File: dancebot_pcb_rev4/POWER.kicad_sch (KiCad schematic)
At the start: 28 parts, among them IC201 TPS63000IDRCRQ1, J201 BatteryJ ST Connector

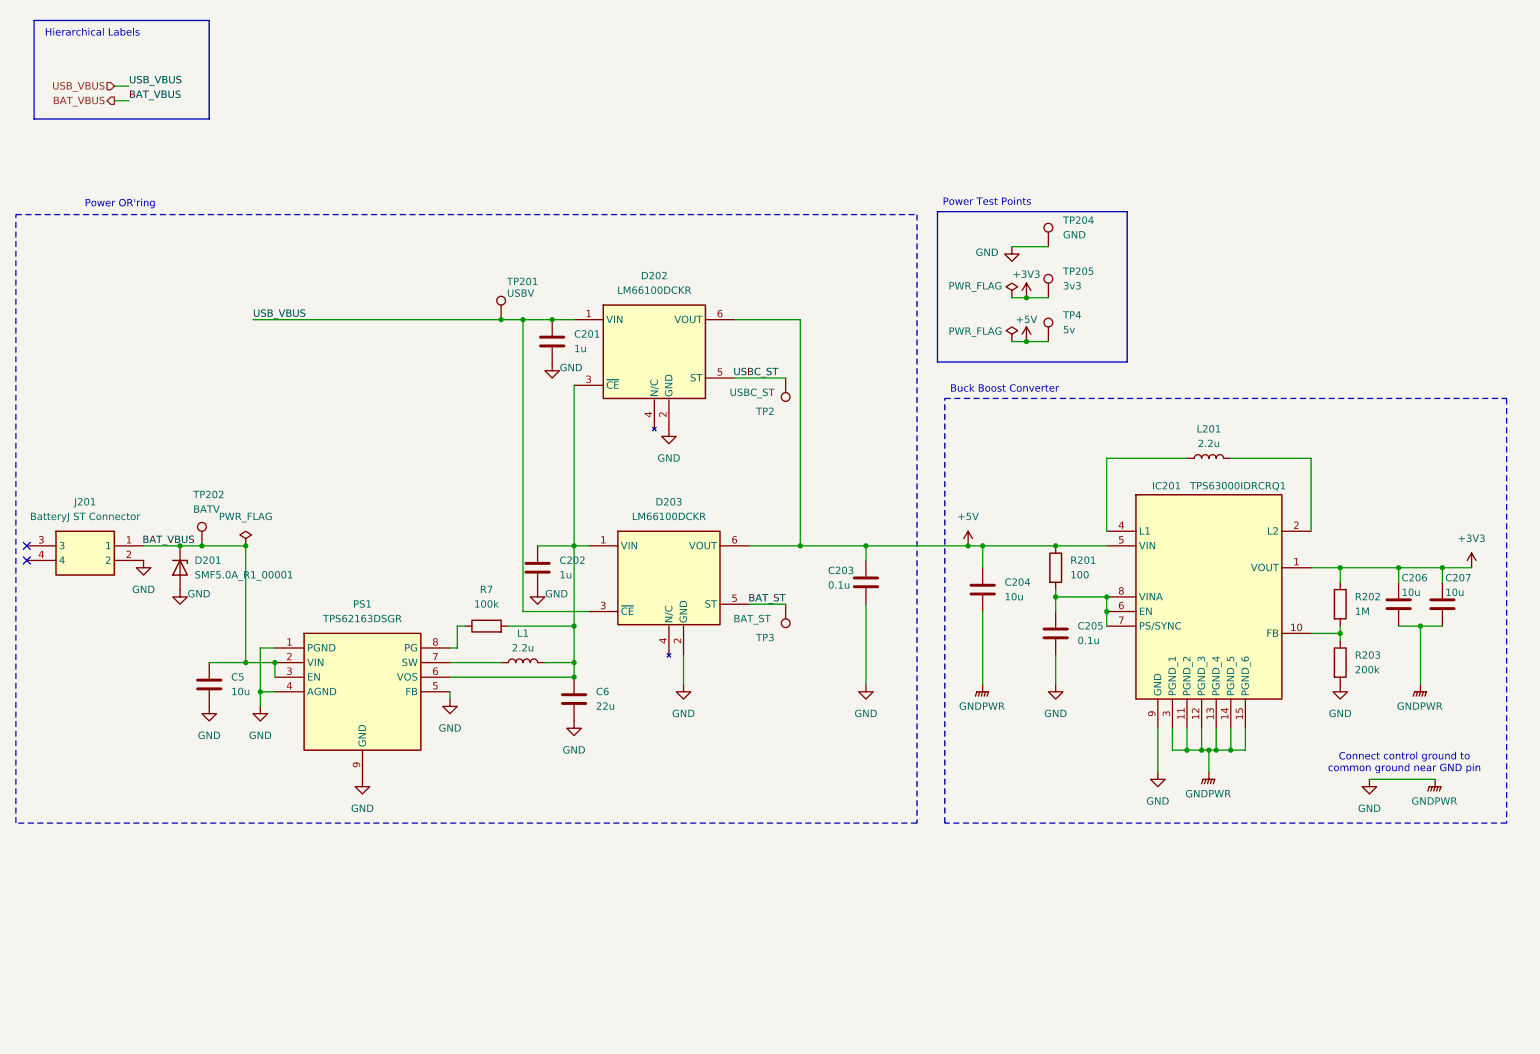
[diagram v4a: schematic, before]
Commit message: added more power leds. need to finish routing. fixed 3d models
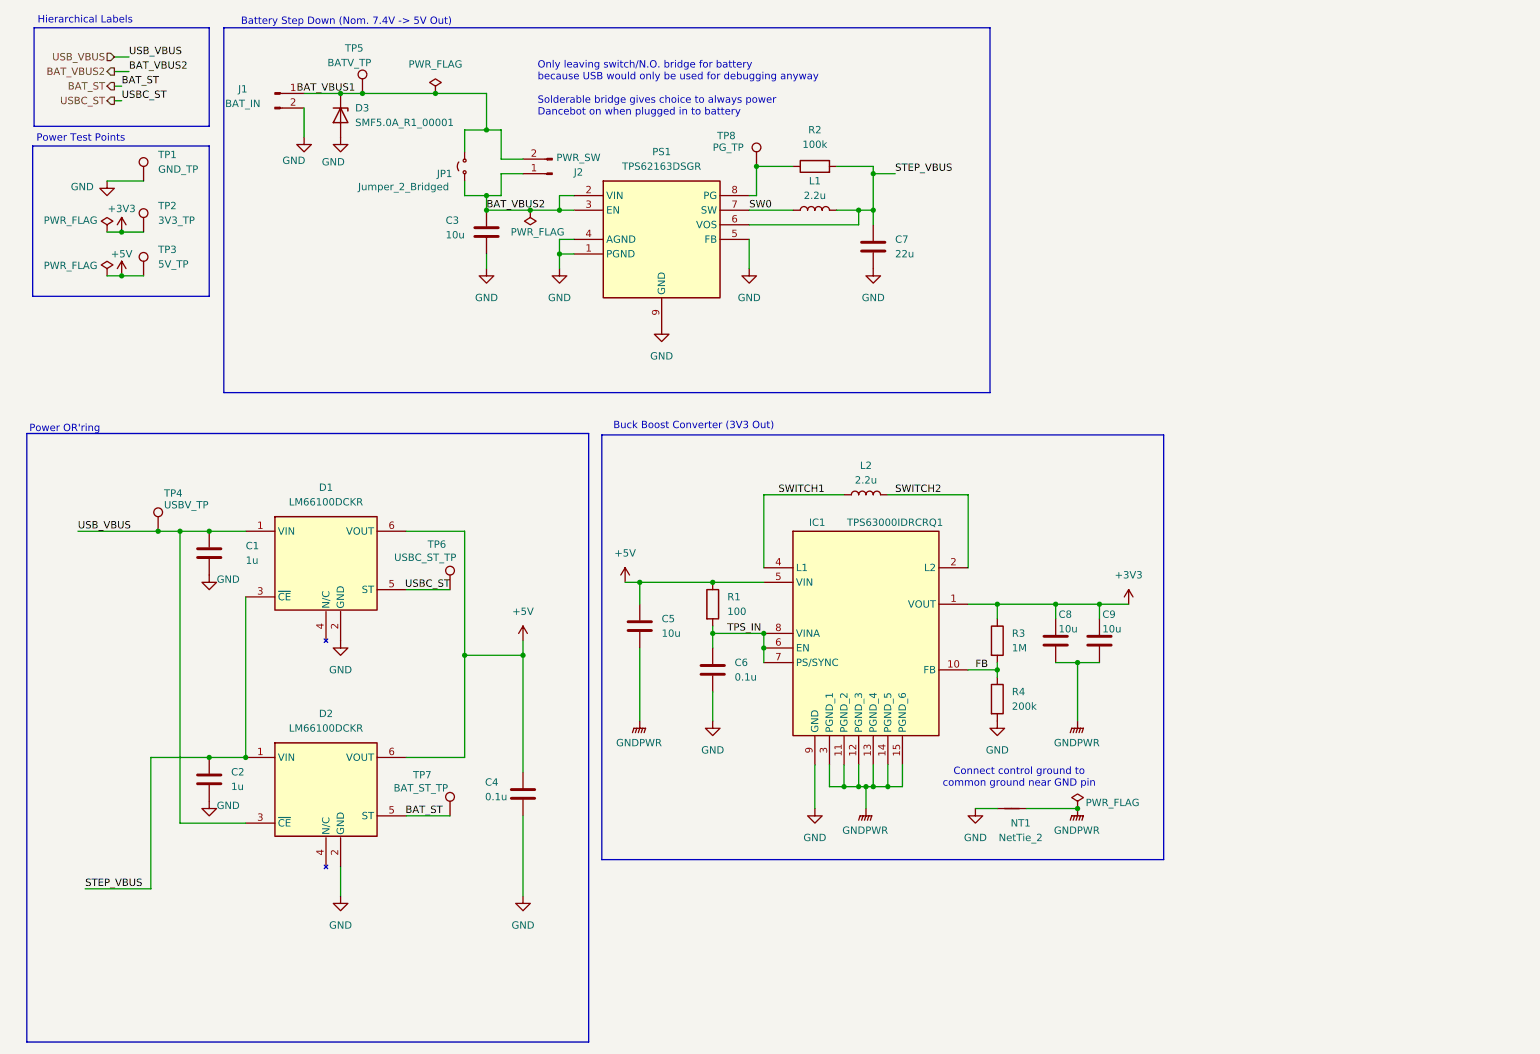
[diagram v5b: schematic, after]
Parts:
- removed C5: 10u, SamacSys_Parts:CAPC1608X80N, symbol Device:C
- removed J201: BatteryJ ST Connector, SamacSys_Parts:1769, symbol SamacSys_Parts:1769
- removed R7: 100k, SamacSys_Parts:RESC2012X50N, symbol Device:R
- added C3: 10u, SamacSys_Parts:CAPC1608X80N, symbol Device:C
- added J1: BAT_IN, Connector_PinHeader_2.00mm:PinHeader_1x02_P2.00mm_Vertical, symbol Connector:Conn_01x02_Pin
- added J2: PWR_SW, Connector_PinHeader_2.00mm:PinHeader_1x02_P2.00mm_Vertical, symbol Connector:Conn_01x02_Pin
- added JP1: Jumper_2_Bridged, Jumper:SolderJumper-2_P1.3mm_Open_RoundedPad1.0x1.5mm, symbol Jumper:Jumper_2_Small_Open
- added NT1: NetTie_2, NetTie:NetTie-2_SMD_Pad0.5mm, symbol Device:NetTie_2
- added R2: 100k, SamacSys_Parts:RESC2012X50N, symbol Device:R
- added TP8: PG_TP, SamacSys_Parts:TestPoint_Pad_1.0x1.0mm, symbol Connector:TestPoint
- C4: renamed from C203; footprint SamacSys_Parts:MAJx16 -> SamacSys_Parts:CAPC2012X140N; Height 0.8 -> 1.4; Manufacturer_Name TAIYO YUDEN -> Kyocera AVX; Manufacturer_Part_Number MAJCU168BB7104KTEA01 -> KAF21KR72A104KL; Mouser Part Number 963-MAJCH168BB7104KT -> 581-KAF21KR72A104KL; Mouser Price/Stock https://www.mouser.co.uk/ProductDetail/TAIYO-YUDEN/MAJCH168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 -> https://www.mouser.co.uk/ProductDetail/KYOCERA-AVX/KAF21KR7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
- C6: renamed from C205; footprint SamacSys_Parts:MAJx16 -> SamacSys_Parts:CAPC2012X140N; Height 0.8 -> 1.4; Manufacturer_Name TAIYO YUDEN -> Kyocera AVX; Manufacturer_Part_Number MAJCU168BB7104KTEA01 -> KAF21KR72A104KL; Mouser Part Number 963-MAJCH168BB7104KT -> 581-KAF21KR72A104KL; Mouser Price/Stock https://www.mouser.co.uk/ProductDetail/TAIYO-YUDEN/MAJCH168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 -> https://www.mouser.co.uk/ProductDetail/KYOCERA-AVX/KAF21KR7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
- C7: renamed from C6; Height (none) -> 1.45; Manufacturer_Name (none) -> TAIYO YUDEN; Manufacturer_Part_Number (none) -> JMK212BBJ226MG8T; Mouser Part Number (none) -> 963-JMK212BBJ226MG8T; Mouser Price/Stock (none) -> https://www.mouser.co.uk/ProductDetail/TAIYO-YUDEN/JMK212BB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
- R4: renamed from R203; footprint SamacSys_Parts:RESC1608X55N -> SamacSys_Parts:RESC2012X60N; Height 0.55 -> 0.6; Manufacturer_Name ROHM Semiconductor -> KOA Speer; Manufacturer_Part_Number KTR03EZPJ204 -> SG73P2ATTD2003F; Mouser Part Number 755-KTR03EZPJ204 -> 660-SG73P2ATTD2003F; Mouser Price/Stock https://www.mouser.co.uk/ProductDetail/ROHM-Semiconductor/K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 -> https://www.mouser.co.uk/ProductDetail/KOA-Speer/SG73P2ATTD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
- TP1: renamed from TP204; value GND -> GND_TP; footprint TestPoint:TestPoint_Pad_1.0x1.0mm -> SamacSys_Parts:TestPoint_Pad_1.0x1.0mm
- TP2: renamed from TP205; value 3v3 -> 3V3_TP; footprint TestPoint:TestPoint_Pad_1.0x1.0mm -> SamacSys_Parts:TestPoint_Pad_1.0x1.0mm
- TP3: renamed from TP4; value 5v -> 5V_TP; footprint TestPoint:TestPoint_Pad_1.0x1.0mm -> SamacSys_Parts:TestPoint_Pad_1.0x1.0mm
- TP4: renamed from TP201; value USBV -> USBV_TP; footprint TestPoint:TestPoint_Pad_1.0x1.0mm -> SamacSys_Parts:TestPoint_Pad_1.0x1.0mm
- TP5: renamed from TP202; value BATV -> BATV_TP; footprint TestPoint:TestPoint_Pad_1.0x1.0mm -> SamacSys_Parts:TestPoint_Pad_1.0x1.0mm
- TP6: renamed from TP2; value USBC_ST -> USBC_ST_TP; footprint TestPoint:TestPoint_Pad_1.0x1.0mm -> SamacSys_Parts:TestPoint_Pad_1.0x1.0mm
- TP7: renamed from TP3; value BAT_ST -> BAT_ST_TP; footprint TestPoint:TestPoint_Pad_1.0x1.0mm -> SamacSys_Parts:TestPoint_Pad_1.0x1.0mm
- renumbered C201 to C1, C202 to C2, C204 to C5, C206 to C8, C207 to C9, D202 to D1, D203 to D2, D201 to D3, IC201 to IC1, L201 to L2, R201 to R1, R202 to R3
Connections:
- net GND: now also C3.2, J1.2 (Pin_2), NT1.1; no longer C5.2, C8.2, C9.2, IC1.11 (PGND_2), IC1.12 (PGND_3), IC1.13 (PGND_4), IC1.14 (PGND_5), IC1.15 (PGND_6), IC1.3 (PGND_1)
- net SW0: now reaches L1.1, PS1.7 (SW)
- net STEP_VBUS: now reaches C2.1, C7.1, D1.3 (~{CE}), D2.1 (VIN), L1.2, PS1.6 (VOS)
- net STEP_VBUS: now also R2.2
- net FB: now reaches IC1.10 (FB), R3.2, R4.1
- net TPS_IN: now reaches C6.1, IC1.6 (EN), IC1.7 (PS/SYNC), IC1.8 (VINA), R1.2
- net at PS1.8 (PG): now also R2.1, TP8.1
- net SWITCH1: now reaches IC1.4 (L1), L2.1
- net SWITCH2: now reaches IC1.2 (L2), L2.2
- net BAT_VBUS renamed BAT_VBUS1
- net BAT_VBUS1: now also J1.1 (Pin_1), J2.2 (Pin_2), JP1.2 (B); no longer PS1.2 (VIN), PS1.3 (EN)
- new net BAT_VBUS2: C3.1, J2.1 (Pin_1), JP1.1 (A), PS1.2 (VIN), PS1.3 (EN)
- new net GNDPWR: C5.2, C8.2, C9.2, IC1.11 (PGND_2), IC1.12 (PGND_3), IC1.13 (PGND_4), IC1.14 (PGND_5), IC1.15 (PGND_6), IC1.3 (PGND_1), NT1.2
- no-connect marks 2 -> 0
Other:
- note added: "Battery Step Down (Nom. 7.4V -> 5V Out)"
- note added: "Buck Boost Converter (3V3 Out)"
- note added: "Only leaving switch/N.O. bridge for battery because USB would only be used for debugging anyway Solderable bridge gives choice to always power Dancebot on when plugged in to battery"
- note removed: "Buck Boost Converter"
- moved on the sheet: C1, C2, C4, C5, C6, C7, C8, C9, D1, D2, D3, IC1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

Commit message: finished first layout. need to add polygon pours
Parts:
- NT1: footprint NetTie:NetTie-2_SMD_Pad0.5mm -> SamacSys_Parts:NetTie-2_SMD_Pad0.3mm
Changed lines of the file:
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@@
 		(on_board yes)
 		(dnp no)
-		(property "Reference" "#PWR04"
+		(property "Reference" "#PWR08"
 			(at 46.99 118.11 0)
 			(effects
@@
 			(project "Dancebot_PCB"
 				(path "/21324b60-e5e7-4de6-a38d-f4cdf81a1b2c/9bb1d94d-135a-4bfe-a8c4-60fef77f5043"
-					(reference "#PWR04")
+					(reference "#PWR08")
 					(unit 1)
 				)
@@
 		(on_board yes)
 		(dnp no)
-		(property "Reference" "#PWR07"
+		(property "Reference" "#PWR011"
 			(at 69.85 41.91 0)
 			(effects
@@
 			(project "Dancebot_PCB"
 				(path "/21324b60-e5e7-4de6-a38d-f4cdf81a1b2c/9bb1d94d-135a-4bfe-a8c4-60fef77f5043"
-					(reference "#PWR07")
+					(reference "#PWR011")
 					(unit 1)
 				)
@@
 		(on_board yes)
 		(dnp no)
-		(property "Reference" "#PWR05"
+		(property "Reference" "#PWR09"
 			(at 46.99 157.48 0)
 			(effects
@@
 			(project "Dancebot_PCB"
 				(path "/21324b60-e5e7-4de6-a38d-f4cdf81a1b2c/9bb1d94d-135a-4bfe-a8c4-60fef77f5043"
-					(reference "#PWR05")
+					(reference "#PWR09")
 					(unit 1)
 				)
@@
 		(dnp no)
 		(fields_autoplaced yes)
-		(property "Reference" "#PWR025"
+		(property "Reference" "#PWR029"
 			(at 198.12 157.48 0)
 			(effects
@@
 			(project "Dancebot_PCB"
 				(path "/21324b60-e5e7-4de6-a38d-f4cdf81a1b2c/9bb1d94d-135a-4bfe-a8c4-60fef77f5043"
-					(reference "#PWR025")
+					(reference "#PWR029")
 					(unit 1)
 				)
@@
 		(on_board yes)
 		(dnp no)
-		(property "Reference" "#FLG05"
+		(property "Reference" "#FLG04"
 			(at 102.87 50.165 0)
 			(effects
@@
 			(project "Dancebot_PCB"
 				(path "/21324b60-e5e7-4de6-a38d-f4cdf81a1b2c/9bb1d94d-135a-4bfe-a8c4-60fef77f5043"
-					(reference "#FLG05")
+					(reference "#FLG04")
 					(unit 1)
 				)
@@
 		(dnp no)
 		(fields_autoplaced yes)
-		(property "Reference" "#PWR08"
+		(property "Reference" "#PWR012"
 			(at 69.85 129.54 0)
 			(effects
@@
 			(project "Dancebot_PCB"
 				(path "/21324b60-e5e7-4de6-a38d-f4cdf81a1b2c/9bb1d94d-135a-4bfe-a8c4-60fef77f5043"
-					(reference "#PWR08")
+					(reference "#PWR012")
 					(unit 1)
 				)
@@
 		(on_board yes)
 		(dnp no)
-		(property "Reference" "#PWR06"
+		(property "Reference" "#PWR010"
 			(at 63.5 41.91 0)
 			(effects
@@
 			(project "Dancebot_PCB"
 				(path "/21324b60-e5e7-4de6-a38d-f4cdf81a1b2c/9bb1d94d-135a-4bfe-a8c4-60fef77f5043"
-					(reference "#PWR06")
+					(reference "#PWR010")
 					(unit 1)
 				)
@@
 		(on_board yes)
 		(dnp no)
-		(property "Reference" "#PWR01"
+		(property "Reference" "#PWR05"
 			(at 29.21 49.53 0)
 			(effects
@@
 			(project "Dancebot_PCB"
 				(path "/21324b60-e5e7-4de6-a38d-f4cdf81a1b2c/9bb1d94d-135a-4bfe-a8c4-60fef77f5043"
-					(reference "#PWR01")
+					(reference "#PWR05")
 					(unit 1)
 				)
@@
 		(dnp no)
 		(fields_autoplaced yes)
-		(property "Reference" "#PWR024"
+		(property "Reference" "#PWR028"
 			(at 198.12 142.24 0)
 			(effects
@@
 			(project "Dancebot_PCB"
 				(path "/21324b60-e5e7-4de6-a38d-f4cdf81a1b2c/9bb1d94d-135a-4bfe-a8c4-60fef77f5043"
-					(reference "#PWR024")
+					(reference "#PWR028")
 					(unit 1)
 				)
@@
 		(dnp no)
 		(fields_autoplaced yes)
-		(property "Reference" "#PWR09"
+		(property "Reference" "#PWR013"
 			(at 69.85 173.99 0)
 			(effects
@@
 			(project "Dancebot_PCB"
 				(path "/21324b60-e5e7-4de6-a38d-f4cdf81a1b2c/9bb1d94d-135a-4bfe-a8c4-60fef77f5043"
-					(reference "#PWR09")
+					(reference "#PWR013")
 					(unit 1)
 				)
@@
 		(dnp no)
 		(fields_autoplaced yes)
-		(property "Reference" "#PWR010"
+		(property "Reference" "#PWR014"
 			(at 95.25 64.77 0)
 			(effects
@@
 			(project ""
 				(path "/21324b60-e5e7-4de6-a38d-f4cdf81a1b2c/9bb1d94d-135a-4bfe-a8c4-60fef77f5043"
-					(reference "#PWR010")
+					(reference "#PWR014")
 					(unit 1)
 				)
@@
 			)
 		)
-		(property "Footprint" "NetTie:NetTie-2_SMD_Pad0.5mm"
+		(property "Footprint" "SamacSys_Parts:NetTie-2_SMD_Pad0.3mm"
 			(at 186.69 152.4 0)
 			(effects
@@
 		(on_board yes)
 		(dnp no)
-		(property "Reference" "#FLG04"
+		(property "Reference" "#FLG05"
 			(at 198.12 150.495 0)
 			(effects
@@
 			(project "Dancebot_PCB"
 				(path "/21324b60-e5e7-4de6-a38d-f4cdf81a1b2c/9bb1d94d-135a-4bfe-a8c4-60fef77f5043"
-					(reference "#FLG04")
+					(reference "#FLG05")
 					(unit 1)
 				)
@@
 		(dnp no)
 		(fields_autoplaced yes)
-		(property "Reference" "#PWR011"
+		(property "Reference" "#PWR015"
 			(at 101.6 127 0)
 			(effects
@@
 			(project "Dancebot_PCB"
 				(path "/21324b60-e5e7-4de6-a38d-f4cdf81a1b2c/9bb1d94d-135a-4bfe-a8c4-60fef77f5043"
-					(reference "#PWR011")
+					(reference "#PWR015")
 					(unit 1)
 				)
@@
 		(dnp no)
 		(fields_autoplaced yes)
-		(property "Reference" "#PWR018"
+		(property "Reference" "#PWR022"
 			(at 140.97 64.77 0)
 			(effects
@@
 			(project ""
 				(path "/21324b60-e5e7-4de6-a38d-f4cdf81a1b2c/9bb1d94d-135a-4bfe-a8c4-60fef77f5043"
-					(reference "#PWR018")
+					(reference "#PWR022")
 					(unit 1)
 				)
@@
 		(dnp no)
 		(fields_autoplaced yes)
-		(property "Reference" "#PWR023"
+		(property "Reference" "#PWR027"
 			(at 184.15 143.51 0)
 			(effects
@@
 			(project "Dancebot_PCB"
 				(path "/21324b60-e5e7-4de6-a38d-f4cdf81a1b2c/9bb1d94d-135a-4bfe-a8c4-60fef77f5043"
-					(reference "#PWR023")
+					(reference "#PWR027")
 					(unit 1)
 				)
@@
 		(dnp no)
 		(fields_autoplaced yes)
-		(property "Reference" "#PWR020"
+		(property "Reference" "#PWR024"
 			(at 161.29 157.48 0)
 			(effects
@@
 			(project "Dancebot_PCB"
 				(path "/21324b60-e5e7-4de6-a38d-f4cdf81a1b2c/9bb1d94d-135a-4bfe-a8c4-60fef77f5043"
-					(reference "#PWR020")
+					(reference "#PWR024")
 					(unit 1)
 				)
@@
 		(dnp no)
 		(fields_autoplaced yes)
-		(property "Reference" "#PWR019"
+		(property "Reference" "#PWR023"
 			(at 152.4 158.75 0)
 			(effects
@@
 			(project "Dancebot_PCB"
 				(path "/21324b60-e5e7-4de6-a38d-f4cdf81a1b2c/9bb1d94d-135a-4bfe-a8c4-60fef77f5043"
-					(reference "#PWR019")
+					(reference "#PWR023")
 					(unit 1)
 				)
@@
 		(dnp no)
 		(fields_autoplaced yes)
-		(property "Reference" "#PWR022"
+		(property "Reference" "#PWR026"
 			(at 180.34 158.75 0)
 			(effects
@@
 			(project "Dancebot_PCB"
 				(path "/21324b60-e5e7-4de6-a38d-f4cdf81a1b2c/9bb1d94d-135a-4bfe-a8c4-60fef77f5043"
-					(reference "#PWR022")
+					(reference "#PWR026")
 					(unit 1)
 				)
@@
 		(dnp no)
 		(fields_autoplaced yes)
-		(property "Reference" "#PWR012"
+		(property "Reference" "#PWR016"
 			(at 101.6 173.99 0)
 			(effects
@@
 			(project "Dancebot_PCB"
 				(path "/21324b60-e5e7-4de6-a38d-f4cdf81a1b2c/9bb1d94d-135a-4bfe-a8c4-60fef77f5043"
-					(reference "#PWR012")
+					(reference "#PWR016")
 					(unit 1)
 				)
@@
 		(dnp no)
 		(fields_autoplaced yes)
-		(property "Reference" "#PWR015"
+		(property "Reference" "#PWR019"
 			(at 121.92 142.24 0)
 			(effects
@@
 			(project "Dancebot_PCB"
 				(path "/21324b60-e5e7-4de6-a38d-f4cdf81a1b2c/9bb1d94d-135a-4bfe-a8c4-60fef77f5043"
-					(reference "#PWR015")
+					(reference "#PWR019")
 					(unit 1)
 				)
@@
 		(dnp no)
 		(fields_autoplaced yes)
-		(property "Reference" "#PWR014"
+		(property "Reference" "#PWR018"
 			(at 119.38 116.84 0)
 			(effects
@@
 			(project ""
 				(path "/21324b60-e5e7-4de6-a38d-f4cdf81a1b2c/9bb1d94d-135a-4bfe-a8c4-60fef77f5043"
-					(reference "#PWR014")
+					(reference "#PWR018")
 					(unit 1)
 				)
@@
 		(on_board yes)
 		(dnp no)
-		(property "Reference" "#PWR03"
+		(property "Reference" "#PWR07"
 			(at 31.75 63.5 0)
 			(effects
@@
 			(project ""
 				(path "/21324b60-e5e7-4de6-a38d-f4cdf81a1b2c/9bb1d94d-135a-4bfe-a8c4-60fef77f5043"
-					(reference "#PWR03")
+					(reference "#PWR07")
 					(unit 1)
 				)
@@
 		(dnp no)
 		(fields_autoplaced yes)
-		(property "Reference" "#PWR021"
+		(property "Reference" "#PWR025"
 			(at 162.56 64.77 0)
 			(effects
@@
 			(project ""
 				(path "/21324b60-e5e7-4de6-a38d-f4cdf81a1b2c/9bb1d94d-135a-4bfe-a8c4-60fef77f5043"
-					(reference "#PWR021")
+					(reference "#PWR025")
 					(unit 1)
 				)
@@
 		(on_board yes)
 		(dnp no)
-		(property "Reference" "#PWR02"
+		(property "Reference" "#PWR06"
 			(at 31.75 55.88 0)
 			(effects
@@
 			(project "Dancebot_PCB"
 				(path "/21324b60-e5e7-4de6-a38d-f4cdf81a1b2c/9bb1d94d-135a-4bfe-a8c4-60fef77f5043"
-					(reference "#PWR02")
+					(reference "#PWR06")
 					(unit 1)
 				)
@@
 		(dnp no)
 		(fields_autoplaced yes)
-		(property "Reference" "#PWR016"
+		(property "Reference" "#PWR020"
 			(at 125.73 74.93 0)
 			(effects
@@
 			(project ""
 				(path "/21324b60-e5e7-4de6-a38d-f4cdf81a1b2c/9bb1d94d-135a-4bfe-a8c4-60fef77f5043"
-					(reference "#PWR016")
+					(reference "#PWR020")
 					(unit 1)
 				)
@@
 		(dnp no)
 		(fields_autoplaced yes)
-		(property "Reference" "#PWR026"
+		(property "Reference" "#PWR030"
 			(at 207.01 120.65 0)
 			(effects
@@
 			(project "Dancebot_PCB"
 				(path "/21324b60-e5e7-4de6-a38d-f4cdf81a1b2c/9bb1d94d-135a-4bfe-a8c4-60fef77f5043"
-					(reference "#PWR026")
+					(reference "#PWR030")
 					(unit 1)
 				)
@@
 		(dnp no)
 		(fields_autoplaced yes)
-		(property "Reference" "#PWR013"
+		(property "Reference" "#PWR017"
 			(at 107.95 64.77 0)
 			(effects
@@
 			(project ""
 				(path "/21324b60-e5e7-4de6-a38d-f4cdf81a1b2c/9bb1d94d-135a-4bfe-a8c4-60fef77f5043"
-					(reference "#PWR013")
+					(reference "#PWR017")
 					(unit 1)
 				)
@@
 		(dnp no)
 		(fields_autoplaced yes)
-		(property "Reference" "#PWR017"
+		(property "Reference" "#PWR021"
 			(at 134.62 143.51 0)
 			(effects
@@
 			(project "Dancebot_PCB"
 				(path "/21324b60-e5e7-4de6-a38d-f4cdf81a1b2c/9bb1d94d-135a-4bfe-a8c4-60fef77f5043"
-					(reference "#PWR017")
+					(reference "#PWR021")
 					(unit 1)
 				)
